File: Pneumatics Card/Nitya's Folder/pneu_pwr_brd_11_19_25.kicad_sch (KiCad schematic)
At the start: 79 parts, among them J1 2X1, J10 Conn_01x02, J11 Conn_01x02, J12 2X1, J13 2X1, J2 2X1, J3 2X1, J4 2X1, J5 2X1, J6 2X1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

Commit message: finished back up pneumatics
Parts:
- removed BOOT_R1: 10k, Resistor_SMD:R_0805_2012Metric_Pad1.20x1.40mm_HandSolder, symbol Device:R_US
- removed Bulk_1: 1uF, Capacitor_SMD:C_0805_2012Metric_Pad1.18x1.45mm_HandSolder, symbol Device:C
- removed Bulk_22: 22uF, Capacitor_SMD:C_0805_2012Metric_Pad1.18x1.45mm_HandSolder, symbol Device:C
- removed Bulk_4.7: 4.7uF, Capacitor_SMD:C_0805_2012Metric_Pad1.18x1.45mm_HandSolder, symbol Device:C
- removed C10, C11: 10pF, Capacitor_SMD:C_0402_1005Metric_Pad0.74x0.62mm_HandSolder, symbol Device:C
- removed C7, C8, C9, T_Cd1, T_Cd2: 100nF, Capacitor_SMD:C_0805_2012Metric_Pad1.18x1.45mm_HandSolder, symbol Device:C
- removed J10, J11: Conn_01x02, Connector_PinHeader_2.54mm:PinHeader_1x02_P2.54mm_Vertical, symbol Connector_Generic:Conn_01x02
- removed J12, J13: 2X1, Connector_JST:JST_PH_B2B-PH-K_1x02_P2.00mm_Vertical, symbol Connector_Generic:Conn_01x02
- removed J7, J9: Conn_01x03_Pin, Connector_PinHeader_2.54mm:PinHeader_1x03_P2.54mm_Vertical, symbol Connector:Conn_01x03_Pin
- removed J8: Conn_01x03, custom_components:slide_switch_EGER1218_Thruster, symbol Connector_Generic:Conn_01x03
- removed U6: STM32G0B1RETx, Package_QFP:LQFP-64_10x10mm_P0.5mm, symbol MCU_ST_STM32G0:STM32G0B1RETx
- removed U7: ATA6561-GAQW-N, custom_components:SOIC8_4P9X3P9MC_MCH, symbol custom_components:ATA6561-GAQW-N
- removed Y1: 16Mhz, Crystal:Crystal_SMD_3225-4Pin_3.2x2.5mm, symbol Device:Crystal_GND24
- added C30: 10u, Capacitor_THT:CP_Radial_D5.0mm_P2.00mm, symbol Device:C
- added R3: 10k, Resistor_SMD:R_0805_2012Metric_Pad1.20x1.40mm_HandSolder, symbol PowerboardRev5-eagle-import:R-US_R0805
- added U10: PCA9685, Package_SO:TSSOP-28_4.4x9.7mm_P0.65mm, symbol New_Library:PCA9685
- R1: value 1k -> 4.7k
- R2: value 4.7k -> 1k
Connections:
- net GND: now also C30.2, R3.2, U10.14 (GND), U10.24 (A5), U10.25 (EXTCLK), U10.3 (A2), U10.4 (A3), U10.5 (A4)
- net S1CTRL: now also U10.6 (PWM0)
- net S2CTRL: now also U10.7 (PWM1)
- net S3CTRL: now also U10.8 (PWM2)
- net S4CTRL: now also U10.9 (PWM3)
- net SCL: now also U10.26 (SCL)
- net SDA: now also U10.27 (SDA)
- new net: R3.1, U10.23 (OE')
- new net +5V: C30.1, U10.1 (A0), U10.2 (A1), U10.28 (VDD)
- no-connect marks 44 -> 0
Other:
- note removed: "CAN Transciever CAN jumper"
- note removed: "HSE"
- note removed: "PWR for STM"
- note removed: "STLINK Flashing"

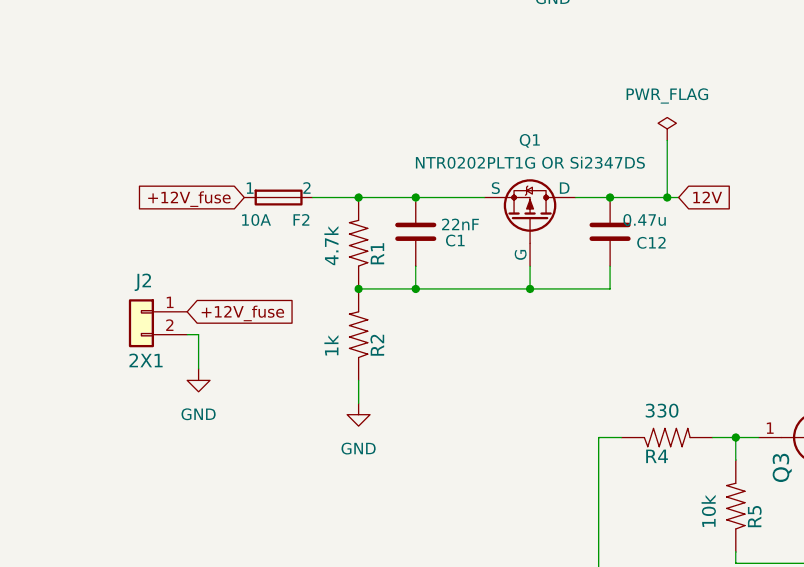
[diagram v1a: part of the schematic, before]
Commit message: Changed resistor values
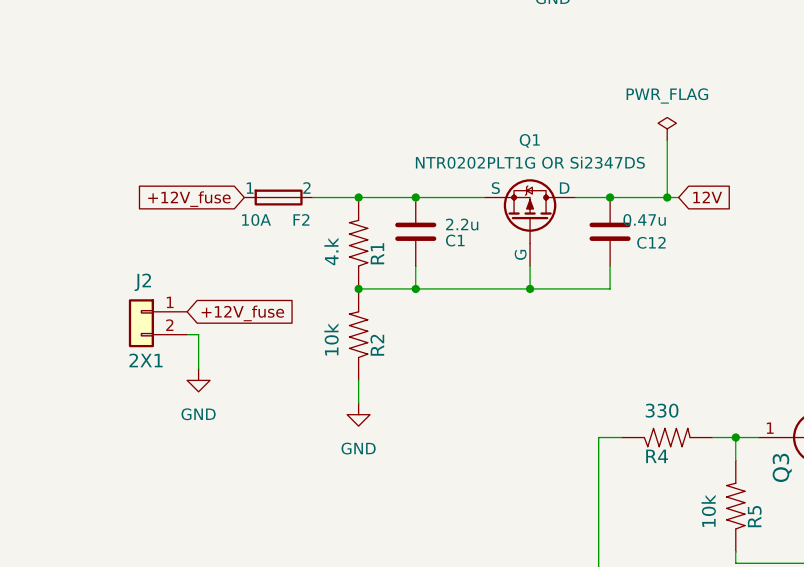
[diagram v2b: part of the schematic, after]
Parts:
- C1: value 22nF -> 2.2u
- R1: value 4.7k -> 4.k
- R2: value 1k -> 10k
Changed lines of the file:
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@@
 			)
 		)
-		(property "Value" "22nF"
+		(property "Value" "2.2u"
 			(at 76.962 119.888 0)
 			(effects
@@
 			)
 		)
-		(property "Value" "1k"
+		(property "Value" "10k"
 			(at 59.69 134.62 0)
 			(effects
@@
 			)
 		)
-		(property "Value" "4.7k"
+		(property "Value" "4.k"
 			(at 59.69 124.46 0)
 			(effects
